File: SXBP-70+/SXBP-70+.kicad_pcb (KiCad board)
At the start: 2 copper layers, 60 x 30 mm, 164 parts, among them U1 SXBP-70+, X1 SMA-F, X2 SMA-F

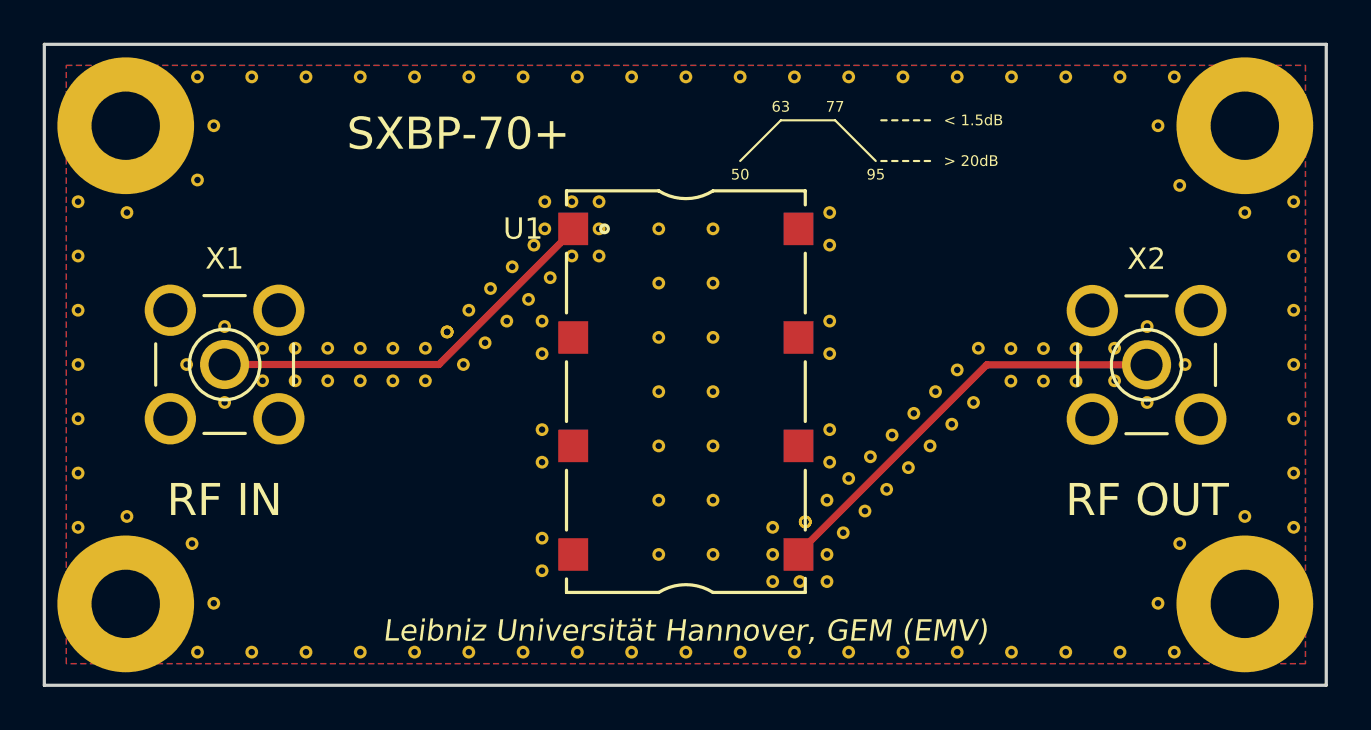
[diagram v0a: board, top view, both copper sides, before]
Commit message: BFCN-70+: corrected 50Ohm CPW, new VIA arrangement
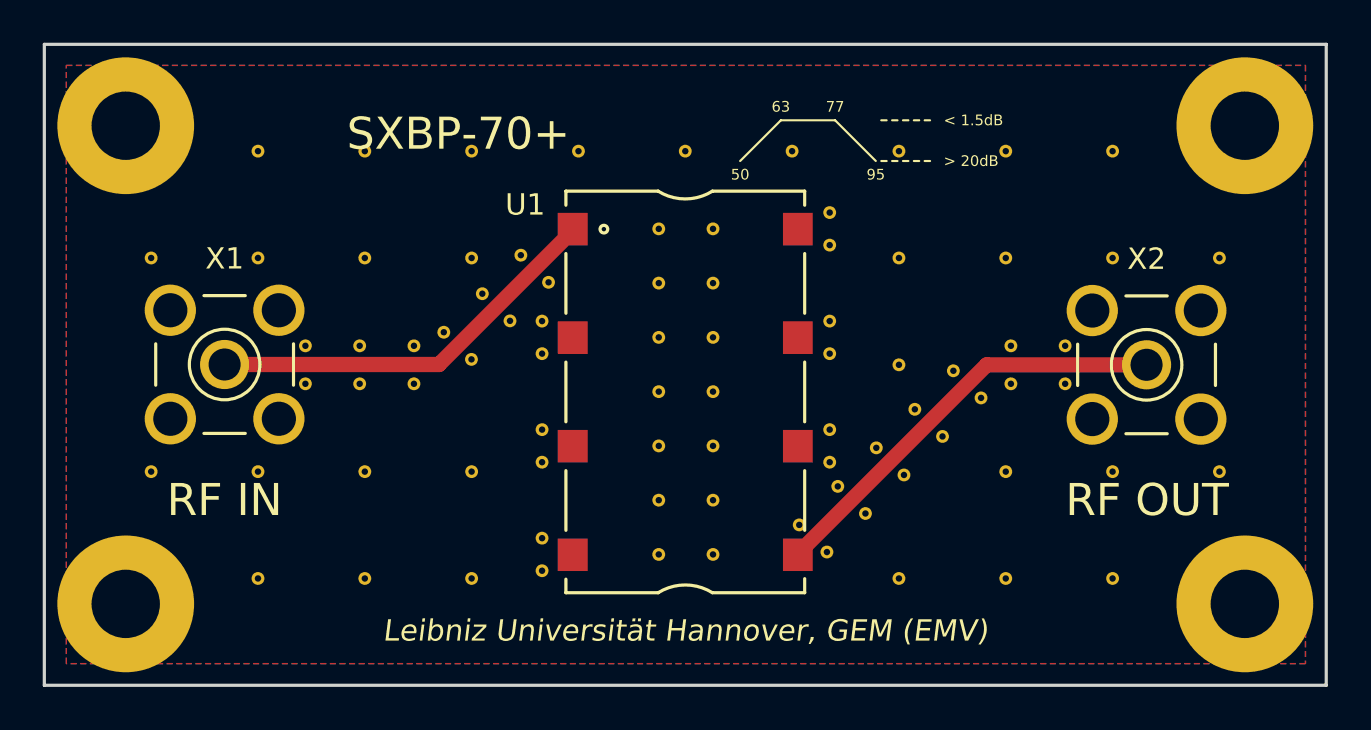
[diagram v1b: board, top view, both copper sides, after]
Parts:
- removed the REF**11 at (108.9, 103.5)
- removed the REF**12 at (101.7, 105.7)
- removed the REF**21 at (135.2, 105.8)
- removed the REF**21 at (130.4, 109.8)
- removed the REF**21 at (129.4, 110.8)
- removed the REF**21 at (128.4, 111.8)
- removed the REF**21 at (127.4, 112.9)
- removed the REF**21 at (126.6, 113.9)
- removed the REF**21 at (126.6, 115.1)
- removed the REF**21 at (125.4, 115.1)
- removed the REF**21 at (124.1, 115.1)
- removed the REF**21 at (124.1, 113.9)
- removed the REF**21 at (124.1, 112.6)
- removed the REF**21 at (136.8, 105.8)
- removed the REF**21 at (125.6, 112.4) (x2)
- removed the REF**21 at (126.6, 111.3)
- removed the REF**21 at (127.6, 110.3)
- removed the REF**21 at (128.7, 109.3)
- removed the REF**21 at (129.7, 108.3)
- removed the REF**21 at (130.7, 107.3)
- removed the REF**21 at (131.7, 106.3)
- removed the REF**21 at (132.7, 105.2)
- removed the REF**21 at (133.7, 104.2)
- removed the REF**21 at (138.3, 105.8)
- removed the REF**21 at (140.1, 105.7)
- removed the REF**21 at (140.1, 104.2)
- removed the REF**21 at (141.6, 103.2)
- removed the REF**21 at (141.6, 106.8)
- removed the REF**21 at (143.4, 105.0)
- removed the REF**21 at (98.4, 103.2)
- removed the REF**21 at (96.7, 105.0)
- removed the REF**21 at (98.4, 106.8)
- removed the REF**21 at (100.2, 105.7)
- removed the REF**21 at (100.2, 104.2)
- removed the REF**21 at (138.3, 104.2)
- removed the REF**21 at (101.7, 104.2)
- removed the REF**21 at (103.3, 104.2)
- removed the REF**21 at (136.8, 104.2)
- removed the REF**21 at (135.2, 104.2)
- removed the REF**21 at (133.5, 106.8)
- removed the REF**21 at (132.5, 107.8)
- removed the REF**21 at (131.5, 108.8)
- removed REF**211 (x2), REF**2111 (x8), REF**2112 (x2), REF**2113 (x2), REF**2114 (x2), REF**2115 (x2), REF**2116 (x2), REF**2117 (x8), REF**221 (x2), REF**231 (x2), REF**241 (x2), REF**251 (x2), REF**261 (x2), REF**2711 (x2), REF**2721 (x2), REF**2731 (x2), REF**2741 (x2), REF**2751 (x2), REF**2761 (x2), REF**27711 (x2), REF**27721 (x2), REF**27731 (x2), REF**27741 (x2), REF**27751 (x2), REF**27761 (x2), REF**27771 (x2), REF**32, REF**41, REF**42, REF**51, REF**52, REF**61, REF**62 (x14), REF**71, REF**72: VIA-0.3, JueVias:VIA-0.3
- removed the REF**22 at (103.3, 105.7)
- removed the REF**31 at (104.8, 104.2)
- added REF**11: VIA-0.3, JueVias:VIA-0.3, F.Cu at (102.2, 104.1)
- added REF**11: VIA-0.3, JueVias:VIA-0.3, F.Cu at (102.2, 105.9)
- added REF**21: VIA-0.3, JueVias:VIA-0.3, F.Cu at (104.8, 104.1)
- added REF**21: VIA-0.3, JueVias:VIA-0.3, F.Cu at (104.8, 105.9)
- added REF**31: VIA-0.3, JueVias:VIA-0.3, F.Cu at (107.3, 104.1)
- added REF**31: VIA-0.3, JueVias:VIA-0.3, F.Cu at (107.3, 105.9)
- added REF**41111: VIA-0.3, JueVias:VIA-0.3, F.Cu at (125.3, 112.5)
- added REF**41111: VIA-0.3, JueVias:VIA-0.3, F.Cu at (108.7, 103.5)
- added REF**41121: VIA-0.3, JueVias:VIA-0.3, F.Cu at (126.6, 113.8)
- added REF**41121: VIA-0.3, JueVias:VIA-0.3, F.Cu at (110.0, 104.7)
- added REF**41122: VIA-0.3, JueVias:VIA-0.3, F.Cu at (127.1, 110.7)
- added REF**41122: VIA-0.3, JueVias:VIA-0.3, F.Cu at (110.5, 101.7)
- added REF**4113102: VIA-0.3, JueVias:VIA-0.3, F.Cu at (135.0, 95.0)
- added REF**4113103: VIA-0.3, JueVias:VIA-0.3, F.Cu at (135.0, 100.0)
- added REF**4113105: VIA-0.3, JueVias:VIA-0.3, F.Cu at (135.0, 110.0)
- added REF**4113106: VIA-0.3, JueVias:VIA-0.3, F.Cu at (135.0, 115.0)
- added REF**4113111: VIA-0.3, JueVias:VIA-0.3, F.Cu at (128.9, 108.9)
- added REF**4113112: VIA-0.3, JueVias:VIA-0.3, F.Cu at (140.0, 95.0)
- added REF**4113113: VIA-0.3, JueVias:VIA-0.3, F.Cu at (140.0, 100.0)
- added REF**4113115: VIA-0.3, JueVias:VIA-0.3, F.Cu at (140.0, 110.0)
- added REF**4113116: VIA-0.3, JueVias:VIA-0.3, F.Cu at (140.0, 115.0)
- added REF**4113122: VIA-0.3, JueVias:VIA-0.3, F.Cu at (130.7, 107.1)
- added REF**4113123: VIA-0.3, JueVias:VIA-0.3, F.Cu at (145.0, 100.0)
- added REF**4113125: VIA-0.3, JueVias:VIA-0.3, F.Cu at (145.0, 110.0)
- added REF**4113133: VIA-0.3, JueVias:VIA-0.3, F.Cu at (132.5, 105.3)
- added REF**41132: VIA-0.3, JueVias:VIA-0.3, F.Cu at (128.4, 112.0)
- added REF**41132: VIA-0.3, JueVias:VIA-0.3, F.Cu at (111.8, 102.9)
- added REF**411323: VIA-0.3, JueVias:VIA-0.3, F.Cu at (95.0, 100.0)
- added REF**411325: VIA-0.3, JueVias:VIA-0.3, F.Cu at (95.0, 110.0)
- added REF**41133: VIA-0.3, JueVias:VIA-0.3, F.Cu at (112.3, 99.9)
- added REF**411332: VIA-0.3, JueVias:VIA-0.3, F.Cu at (100.0, 95.0)
- added REF**411333: VIA-0.3, JueVias:VIA-0.3, F.Cu at (100.0, 100.0)
- added REF**411335: VIA-0.3, JueVias:VIA-0.3, F.Cu at (100.0, 110.0)
- added REF**411336: VIA-0.3, JueVias:VIA-0.3, F.Cu at (100.0, 115.0)
- added REF**411342: VIA-0.3, JueVias:VIA-0.3, F.Cu at (105.0, 95.0)
- added REF**411343: VIA-0.3, JueVias:VIA-0.3, F.Cu at (105.0, 100.0)
- added REF**411345: VIA-0.3, JueVias:VIA-0.3, F.Cu at (105.0, 110.0)
- added REF**411346: VIA-0.3, JueVias:VIA-0.3, F.Cu at (105.0, 115.0)
- added REF**411352: VIA-0.3, JueVias:VIA-0.3, F.Cu at (110.0, 95.0)
- added REF**411353: VIA-0.3, JueVias:VIA-0.3, F.Cu at (110.0, 100.0)
- added REF**411355: VIA-0.3, JueVias:VIA-0.3, F.Cu at (110.0, 110.0)
- added REF**411356: VIA-0.3, JueVias:VIA-0.3, F.Cu at (110.0, 115.0)
- added REF**411362: VIA-0.3, JueVias:VIA-0.3, F.Cu at (115.0, 95.0)
- added REF**411372: VIA-0.3, JueVias:VIA-0.3, F.Cu at (120.0, 95.0)
- added REF**411382: VIA-0.3, JueVias:VIA-0.3, F.Cu at (125.0, 95.0)
- added REF**411392: VIA-0.3, JueVias:VIA-0.3, F.Cu at (130.0, 95.0)
- added REF**411393: VIA-0.3, JueVias:VIA-0.3, F.Cu at (130.0, 100.0)
- added REF**411394: VIA-0.3, JueVias:VIA-0.3, F.Cu at (130.0, 105.0)
- added REF**411396: VIA-0.3, JueVias:VIA-0.3, F.Cu at (130.0, 115.0)
- added REF**411411: VIA-0.3, JueVias:VIA-0.3, F.Cu at (130.2, 110.2)
- added REF**411422: VIA-0.3, JueVias:VIA-0.3, F.Cu at (132.0, 108.4)
- added REF**41143: VIA-0.3, JueVias:VIA-0.3, F.Cu at (113.6, 101.1)
- added REF**4114311: VIA-0.3, JueVias:VIA-0.3, F.Cu at (135.2, 105.9)
- added REF**4114311: VIA-0.3, JueVias:VIA-0.3, F.Cu at (135.2, 104.1)
- added REF**4114321: VIA-0.3, JueVias:VIA-0.3, F.Cu at (137.8, 105.9)
- added REF**4114321: VIA-0.3, JueVias:VIA-0.3, F.Cu at (137.8, 104.1)
- added REF**411433: VIA-0.3, JueVias:VIA-0.3, F.Cu at (133.8, 106.5)
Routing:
- net (no net): track 120.0 -> 90.0 mm
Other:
- net class 50Ohm: clearance 0.2 -> 0.15; trace_width 0.336 -> 0.714
- net class Default: clearance 0.1 -> 0.15
- rule trace_clearance: 0.1 -> 0.15
